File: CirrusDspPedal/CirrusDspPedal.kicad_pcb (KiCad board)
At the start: 2 copper layers, 112.5 x 86.4 mm, 5 parts

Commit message: updates
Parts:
- removed the REF** at (198.8, 62.2)
- removed the REF** at (111.1, 62.2)
- removed the REF** at (111.1, 135.9)
- added C1: 100nF, Capacitor_SMD:C_0805_2012Metric_Pad1.15x1.40mm_HandSolder, F.Cu at (215.3, 126.4)
- added C10: 100nF, Capacitor_SMD:C_0805_2012Metric_Pad1.15x1.40mm_HandSolder, F.Cu at (74.3, 143.5)
- added C11: 1uF, Capacitor_SMD:C_0805_2012Metric_Pad1.15x1.40mm_HandSolder, F.Cu at (79.4, 143.5)
- added C12: 3.3uF, Capacitor_SMD:C_0805_2012Metric_Pad1.15x1.40mm_HandSolder, F.Cu at (67.3, 121.3)
- added C13: 10uF, Capacitor_SMD:C_0805_2012Metric_Pad1.15x1.40mm_HandSolder, F.Cu at (69.2, 143.5)
- added C14: 2.7nF, Capacitor_SMD:C_0805_2012Metric_Pad1.15x1.40mm_HandSolder, F.Cu at (72.2, 120.9)
- added C15: 100nF, Capacitor_SMD:C_0805_2012Metric_Pad1.15x1.40mm_HandSolder, F.Cu at (76.4, 135.7)
- added C16: 100nF, Capacitor_SMD:C_0805_2012Metric_Pad1.15x1.40mm_HandSolder, F.Cu at (71.7, 135.7)
- added C17: 100nF, Capacitor_SMD:C_0805_2012Metric_Pad1.15x1.40mm_HandSolder, F.Cu at (71.7, 138.7)
- added C18: 100nF, Capacitor_SMD:C_0805_2012Metric_Pad1.15x1.40mm_HandSolder, F.Cu at (141.6, -22.2)
- added C19: 100nF, Capacitor_SMD:C_0805_2012Metric_Pad1.15x1.40mm_HandSolder, F.Cu at (141.6, -19.7)
- added C2: 1uF, Capacitor_SMD:C_0805_2012Metric_Pad1.15x1.40mm_HandSolder, F.Cu at (215.3, 123.8)
- added C20: 100nF, Capacitor_SMD:C_0805_2012Metric_Pad1.15x1.40mm_HandSolder, F.Cu at (141.6, -17.1)
- added C21: 100nF, Capacitor_SMD:C_0805_2012Metric_Pad1.15x1.40mm_HandSolder, F.Cu at (141.6, -14.6)
- added C22: 2.2uF, Capacitor_SMD:C_0805_2012Metric_Pad1.15x1.40mm_HandSolder, F.Cu at (146.7, -22.2)
- added C28: 1uF, Capacitor_SMD:C_1206_3216Metric_Pad1.42x1.75mm_HandSolder, F.Cu at (130.8, 44.5)
- added C29: 1uF, Capacitor_SMD:C_1206_3216Metric_Pad1.42x1.75mm_HandSolder, F.Cu at (123.2, 38.1)
- added C3: 10uF, Capacitor_SMD:C_0805_2012Metric_Pad1.15x1.40mm_HandSolder, F.Cu at (215.3, 128.9)
- added C30: 180pF C0G, Capacitor_SMD:C_0805_2012Metric_Pad1.15x1.40mm_HandSolder, F.Cu at (176.5, 39.4)
- added C31: 180pF C0G, Capacitor_SMD:C_0805_2012Metric_Pad1.15x1.40mm_HandSolder, F.Cu at (235.6, 77.5)
- added C32: 180pF C0G, Capacitor_SMD:C_0805_2012Metric_Pad1.15x1.40mm_HandSolder, F.Cu at (76.2, 71.8)
- added C33: 2.2uF, Capacitor_SMD:C_0805_2012Metric_Pad1.15x1.40mm_HandSolder, F.Cu at (146.7, -18.4)
- added C4: 1uF, Capacitor_SMD:C_0805_2012Metric_Pad1.15x1.40mm_HandSolder, F.Cu at (228.0, 130.3)
- added C5: 180pF C0G, Capacitor_SMD:C_0805_2012Metric_Pad1.15x1.40mm_HandSolder, F.Cu at (228.0, 132.7)
- added C6: 100nF, Capacitor_SMD:C_0805_2012Metric_Pad1.15x1.40mm_HandSolder, F.Cu at (215.3, 131.4)
- added C7: 100nF, Capacitor_SMD:C_0805_2012Metric_Pad1.15x1.40mm_HandSolder, F.Cu at (232.2, 138.3)
- added C8: 100nF, Capacitor_SMD:C_0805_2012Metric_Pad1.15x1.40mm_HandSolder, F.Cu at (237.0, 138.3)
- added C9: 100nF, Capacitor_SMD:C_0805_2012Metric_Pad1.15x1.40mm_HandSolder, F.Cu at (237.0, 141.2)
- added D1: D_Schottky, Diode_SMD:D_SOD-123F, F.Cu at (121.9, 44.5)
- added D2: 1N4148, Diode_SMD:D_SOD-123F, F.Cu at (143.9, 105.6)
- added FB1: 600, Inductor_SMD:L_0805_2012Metric_Pad1.15x1.40mm_HandSolder, F.Cu at (232.2, 141.2)
- added FB2: 600, Inductor_SMD:L_0805_2012Metric_Pad1.15x1.40mm_HandSolder, F.Cu at (76.4, 138.7)
- added J1: MonoJack2Switch, NeutrikNRJ:NRJxHx_NOTAB, F.Cu at (193.7, 110.5)
- added J2: MonoJack2Switch, NeutrikNRJ:NRJxHx_NOTAB, F.Cu at (103.5, 110.5)
- added J3: Conn_02x05_Odd_Even, Connector_PinHeader_1.27mm:PinHeader_2x05_P1.27mm_Vertical_SMD, F.Cu at (113.4, -18.9)
- added J4: Barrel_Jack_Switch, Connector_BarrelJack:BarrelJack_Horizontal, F.Cu at (129.5, 68.6)
- added J5: MonoJack2Switch, NeutrikNRJ:NRJxHx_NOTAB, F.Cu at (171.4, 66.7)
- added J6: Micro_SD_Card_Det, Connector_Card:microSD_HC_Molex_104031-0811, F.Cu at (230.5, -22.2)
- added J7: Conn_01x01, TestPoint:TestPoint_Pad_2.0x2.0mm, F.Cu at (259.7, -15.9)
- added JP1: Jumper_NC_Small, Jumper:SolderJumper-2_P1.3mm_Bridged_Pad1.0x1.5mm, F.Cu at (230.5, -4.45)
- added K1: HFD4/5-S, Relay_SMD:Relay_Fujitsu_FTR-B3S, F.Cu at (148.3, 113.3)
- added L1: 600, Inductor_SMD:L_0805_2012Metric_Pad1.15x1.40mm_HandSolder, F.Cu at (146.7, -15.9)
- added LED1: LED_RABG, LED_THT:LED_D5.0mm-4_RGB_Wide_Pins, F.Cu at (81.9, 3.17)
- added LED2: LED_RABG, LED_THT:LED_D5.0mm-4_RGB_Wide_Pins, F.Cu at (111.1, 1.91)
- added R1: 5K1, Resistor_SMD:R_0805_2012Metric_Pad1.15x1.40mm_HandSolder, F.Cu at (222.9, 132.7)
- added R10: 1K, Resistor_SMD:R_0805_2012Metric_Pad1.15x1.40mm_HandSolder, F.Cu at (156.8, 151.1)
- added R11: 100R, Resistor_SMD:R_0805_2012Metric_Pad1.15x1.40mm_HandSolder, F.Cu at (235.6, 81.3)
- added R12: 100R, Resistor_SMD:R_0805_2012Metric_Pad1.15x1.40mm_HandSolder, F.Cu at (76.2, 76.8)
- added R13: 50R, Resistor_SMD:R_0805_2012Metric_Pad1.15x1.40mm_HandSolder, F.Cu at (235.6, 85.1)
- added R14: 50R, Resistor_SMD:R_0805_2012Metric_Pad1.15x1.40mm_HandSolder, F.Cu at (76.2, 80.6)
- added R15: 1K, Resistor_SMD:R_0805_2012Metric_Pad1.15x1.40mm_HandSolder, F.Cu at (255.9, 81.9)
- added R16: 1K, Resistor_SMD:R_0805_2012Metric_Pad1.15x1.40mm_HandSolder, F.Cu at (47.6, 76.8)
- added R17: 220R, Resistor_SMD:R_0805_2012Metric_Pad1.15x1.40mm_HandSolder, F.Cu at (75.6, -0.64)
- added R18: 220R, Resistor_SMD:R_0805_2012Metric_Pad1.15x1.40mm_HandSolder, F.Cu at (75.6, 3.17)
- added R19: 220R, Resistor_SMD:R_0805_2012Metric_Pad1.15x1.40mm_HandSolder, F.Cu at (75.6, 6.99)
- added R2: 5K1, Resistor_SMD:R_0805_2012Metric_Pad1.15x1.40mm_HandSolder, F.Cu at (222.9, 130.2)
- added R20: 220R, Resistor_SMD:R_0805_2012Metric_Pad1.15x1.40mm_HandSolder, F.Cu at (104.8, -1.91)
- added R21: 220R, Resistor_SMD:R_0805_2012Metric_Pad1.15x1.40mm_HandSolder, F.Cu at (104.8, 1.91)
- added R22: 220R, Resistor_SMD:R_0805_2012Metric_Pad1.15x1.40mm_HandSolder, F.Cu at (104.8, 5.71)
- added R23: 10K, Resistor_SMD:R_0805_2012Metric_Pad1.15x1.40mm_HandSolder, F.Cu at (225.0, -11.4)
- added R24: 47K, Resistor_SMD:R_0805_2012Metric_Pad1.15x1.40mm_HandSolder, F.Cu at (225.0, -8.46)
- added R25: 47K, Resistor_SMD:R_0805_2012Metric_Pad1.15x1.40mm_HandSolder, F.Cu at (229.8, -11.4)
- added R26: 47K, Resistor_SMD:R_0805_2012Metric_Pad1.15x1.40mm_HandSolder, F.Cu at (234.3, -8.26)
- added R27: 47K, Resistor_SMD:R_0805_2012Metric_Pad1.15x1.40mm_HandSolder, F.Cu at (229.8, -8.46)
- added R28: 47K, Resistor_SMD:R_0805_2012Metric_Pad1.15x1.40mm_HandSolder, F.Cu at (234.5, -11.4)
- added R3: 10K, Resistor_SMD:R_0805_2012Metric_Pad1.15x1.40mm_HandSolder, F.Cu at (228.0, 123.8)
- added R4: 1R 1%, Resistor_SMD:R_0805_2012Metric_Pad1.15x1.40mm_HandSolder, F.Cu at (241.7, 138.3)
- added R5: 10K, Resistor_SMD:R_0805_2012Metric_Pad1.15x1.40mm_HandSolder, F.Cu at (72.2, 123.9)
- added R6: 470 1%, Resistor_SMD:R_0805_2012Metric_Pad1.15x1.40mm_HandSolder, F.Cu at (76.9, 120.9)
- added R7: 1R 1%, Resistor_SMD:R_0805_2012Metric_Pad1.15x1.40mm_HandSolder, F.Cu at (81.2, 135.7)
- added R8: 50R, Resistor_SMD:R_0805_2012Metric_Pad1.15x1.40mm_HandSolder, F.Cu at (176.5, 36.8)
- added R9: 1K, Resistor_SMD:R_0805_2012Metric_Pad1.15x1.40mm_HandSolder, F.Cu at (142.9, 150.5)
- added REF**: MountingHole_4mm_Pad_Via, MountingHole:MountingHole_4mm_Pad_Via, F.Cu at (192.4, 60.9)
- added REF**: MountingHole_4mm_Pad_Via, MountingHole:MountingHole_4mm_Pad_Via, F.Cu at (104.8, 60.9)
- added REF**: MountingHole_4mm_Pad_Via, MountingHole:MountingHole_4mm_Pad_Via, F.Cu at (104.8, 134.6)
- added RV1: R_POT, Potentiometer_THT:Potentiometer_Alps_RK09L_Single_Vertical, F.Cu at (226.7, 87.6)
- added RV2: R_POT, Potentiometer_THT:Potentiometer_Alps_RK09L_Single_Vertical, F.Cu at (67.3, 81.9)
- added SW1: P26L-1D-RND MTL, Connector_PinSocket_2.54mm:PinSocket_1x02_P2.54mm_Vertical, F.Cu at (144.8, 134.6)
- added SW2: P26L-1D-RND MTL, Connector_PinSocket_2.54mm:PinSocket_1x02_P2.54mm_Vertical, F.Cu at (153.7, 135.9)
- added SW3: SW_SPST, custom_sw:SW_SPDT_W6.86MM_L12.7MM_P4.8MM_D2MM, F.Cu at (250.1, 81.5)
- added SW4: SW_SPST, custom_sw:SW_SPDT_W6.86MM_L12.7MM_P4.8MM_D2MM, F.Cu at (41.9, 77.5)
- added U1: CS5343, Package_SO:TSSOP-10_3x3mm_P0.5mm, F.Cu at (225.4, 140.3)
- added U2: 74AHC1G126, Package_TO_SOT_SMD:SOT-23-5_HandSoldering, F.Cu at (223.4, 123.8)
- added U3: CS4344, Package_SO:TSSOP-10_3x3mm_P0.5mm, F.Cu at (75.2, 130.2)
- added U5: MCP1700-3302E_SOT23, Package_TO_SOT_SMD:SOT-23, F.Cu at (133.3, 36.8)
- added U6: MCP601-xOT, Package_TO_SOT_SMD:SOT-23-5, F.Cu at (171.4, 38.1)
- added U7: STM32F405RGTx, Package_QFP:LQFP-64_10x10mm_P0.5mm, F.Cu at (130.7, -18.9)
- moved REF** 6.48 mm to (148.6, 97.8)
- moved REF** 6.48 mm to (192.4, 134.6)
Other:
- outline, holes or cut-outs redrawn

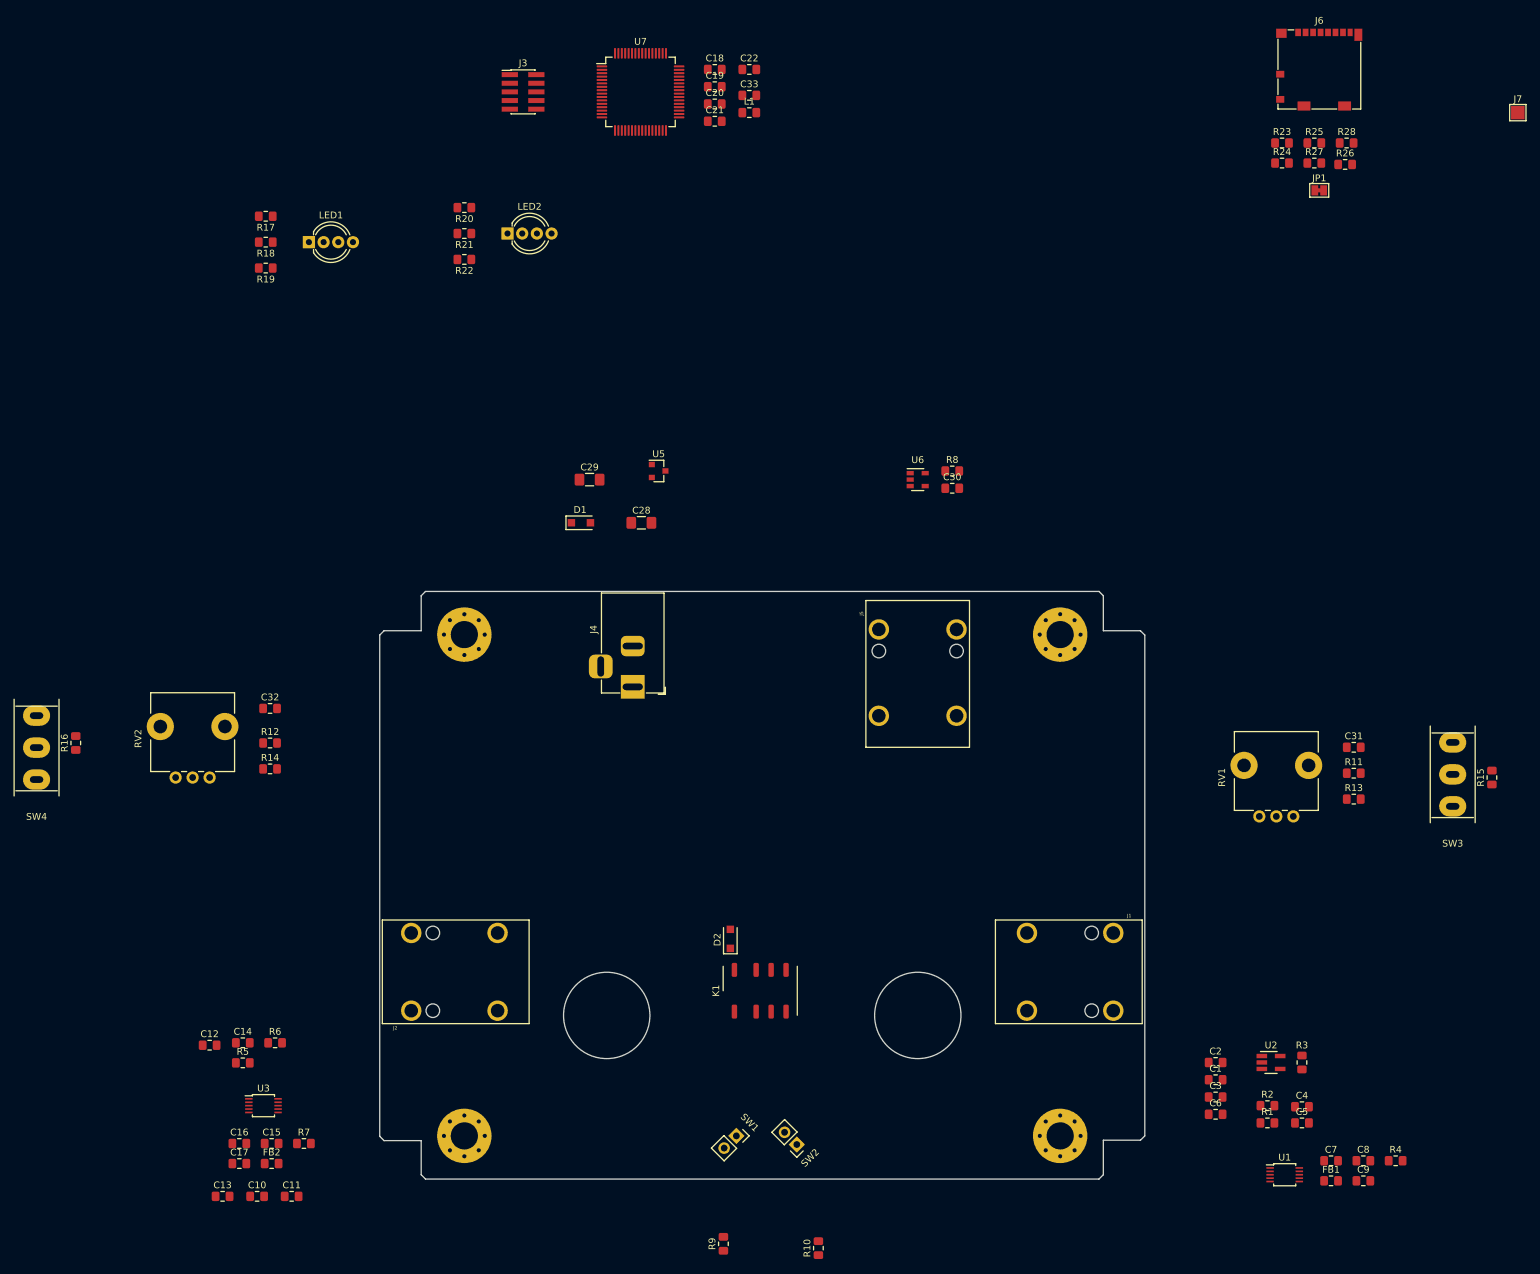
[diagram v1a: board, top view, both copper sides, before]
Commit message: finished RevA layout
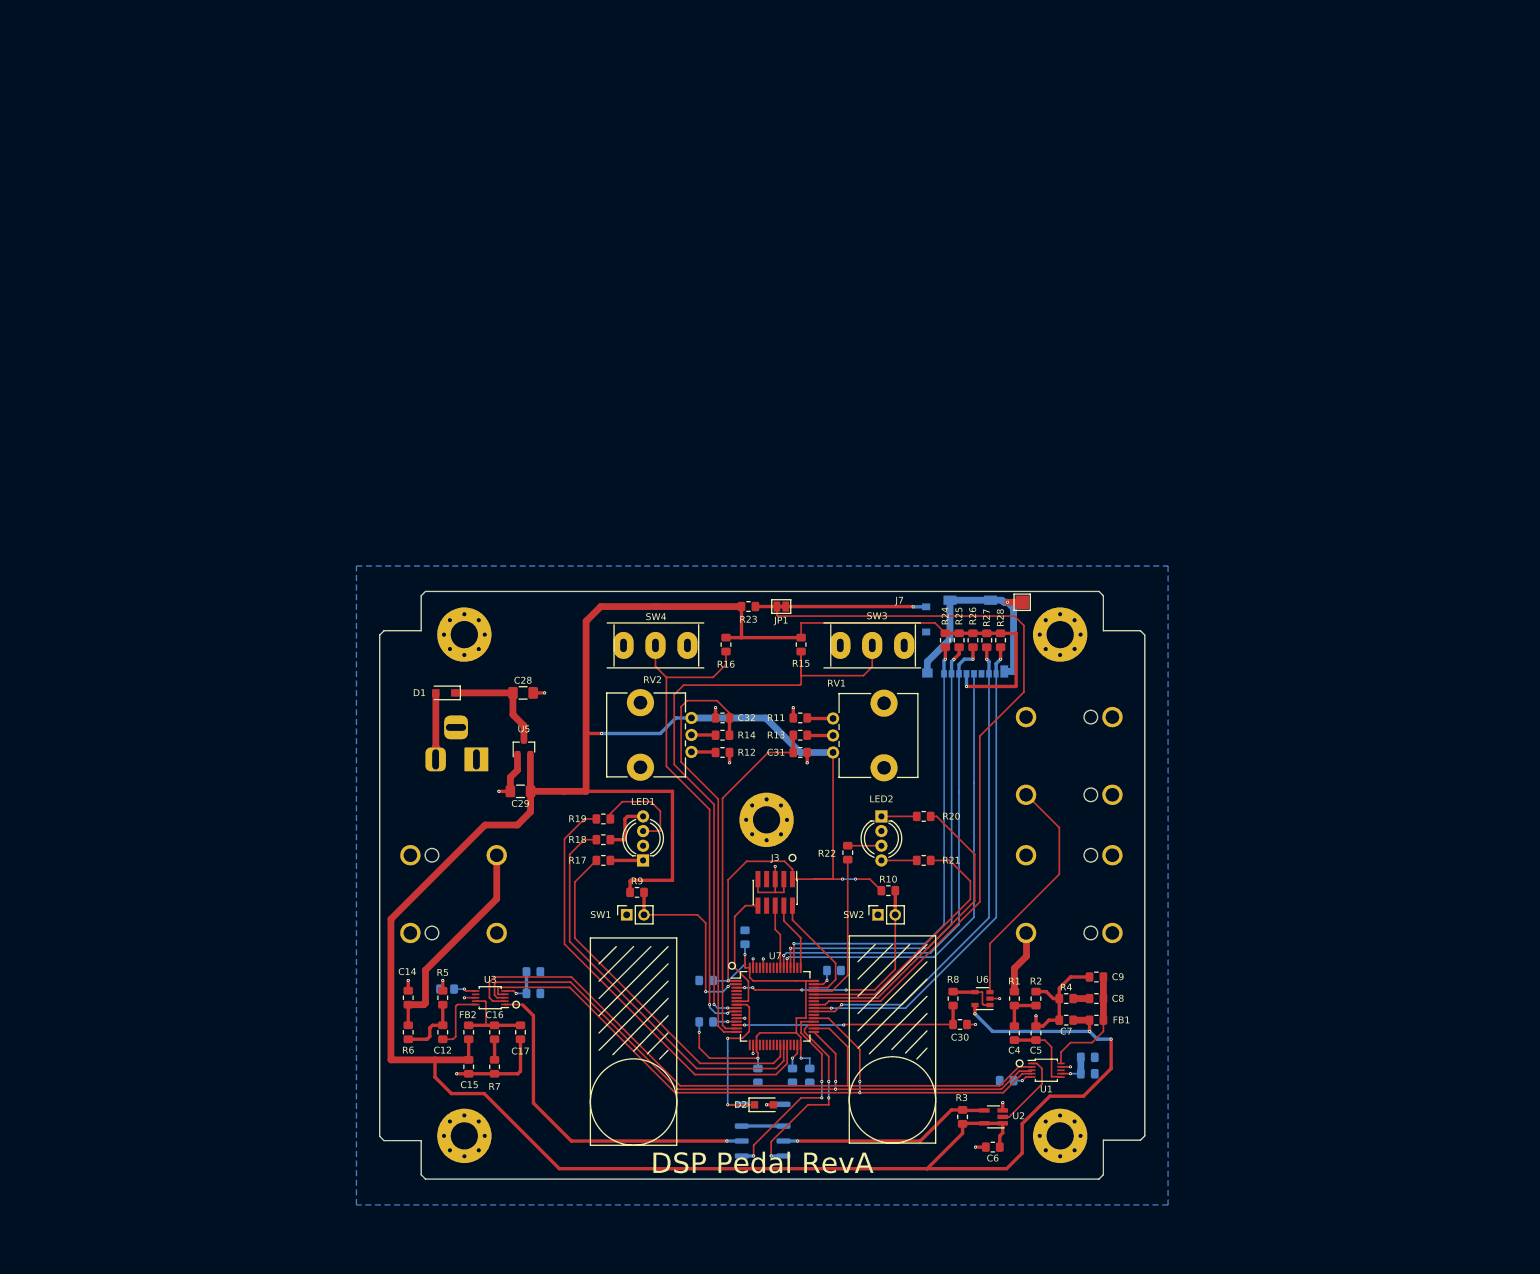
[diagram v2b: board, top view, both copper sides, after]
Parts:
- added REF**: MountingHole_4mm_Pad_Via, MountingHole:MountingHole_4mm_Pad_Via, F.Cu at (149.2, 88.1)
- C1, C10, C11, C13, C18, C19, C2, C20, C21, C22, C3, C33, J1, J2, J4, J5, J6, K1, L1: moved to B.Cu
- moved C22 148.1 mm to (153.0, 125.7), turned to 90 degrees
- moved C19 146.1 mm to (155.6, 125.7), turned to 270 degrees
- moved C20 143.0 mm to (148.0, 125.7), turned to 270 degrees
- moved U7 135.9 mm to (150.5, 115.6)
- moved C18 134.0 mm to (140.3, 111.8), turned to 180 degrees
- moved L1 133.9 mm to (140.3, 117.9)
- moved C33 129.3 mm to (159.1, 110.3), turned to 180 degrees
- moved J3 123.4 mm to (150.5, 98.8), turned to 270 degrees
- moved C21 120.1 mm to (146.1, 105.4), turned to 90 degrees
- moved R21 114.3 mm to (172.3, 94.1), turned to 0 degrees
- moved R20 112.2 mm to (172.3, 87.6), turned to 0 degrees
- moved R17 107.0 mm to (125.2, 94.1)
- moved R23 104.0 mm to (146.6, 56.8)
- moved R22 103.9 mm to (161.2, 93.0), turned to 270 degrees
- moved R15 103.5 mm to (154.3, 62.4), turned to 270 degrees
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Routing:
- net +3V3: track 0.00 -> 562.4 mm, vias 0 -> 12
- net /MicroSD/uSD_Detect: track 0.00 -> 115.4 mm
- net /InputSignal/ADIN_SCLK: track 0.00 -> 104.5 mm
- net /InputSignal/ADIN_MCLK: track 0.00 -> 103.1 mm, vias 0 -> 2
- net /InputSignal/ADIN_LRCK: track 0.00 -> 99.9 mm, vias 0 -> 2
- net /ExtInput/UserSwitchA_IN: track 0.00 -> 93.4 mm, vias 0 -> 2
- net GND: track 0.00 -> 77.6 mm, vias 0 -> 22
- net /MicroSD/uSD_D1: track 0.00 -> 72.7 mm, vias 0 -> 2
- net /ExtInput/UserSwitchB_IN: track 0.00 -> 72.4 mm, vias 0 -> 2
- net /MicroSD/uSD_CMD: track 0.00 -> 71.8 mm, vias 0 -> 2
- net /MicroSD/uSD_D0: track 0.00 -> 71.6 mm, vias 0 -> 2
- net /MicroSD/uSD_D3: track 0.00 -> 69.2 mm, vias 0 -> 2
- net /MicroSD/uSD_D2: track 0.00 -> 67.9 mm, vias 0 -> 2
- net /MicroSD/uSD_CLK: track 0.00 -> 67.1 mm, vias 0 -> 1
- net /SignalProcessing/LEDA_B: track 0.00 -> 65.5 mm
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- added copper zone on B.Cu, net GND
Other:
- outline, holes or cut-outs redrawn
- net class Default: clearance 0.2 -> 0.127; trace_width 0.25 -> 0.127
- rule trace_clearance: 0.2 -> 0.127
- rule trace_min: 0.2 -> 0.127
- rule via_min_drill: 0.3 -> 0.2
- rule via_min_size: 0.4 -> 0.45
- board text added: "DSP Pedal RevA"

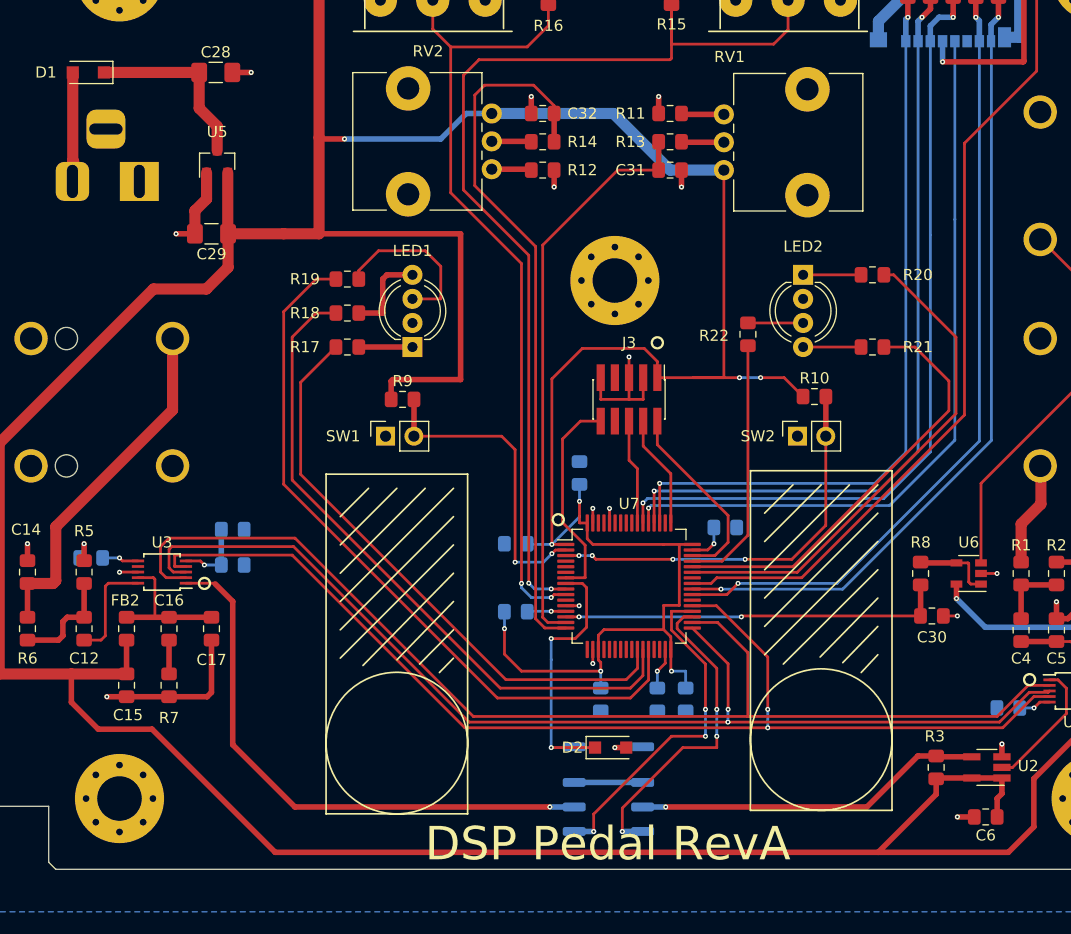
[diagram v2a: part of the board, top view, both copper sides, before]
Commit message: updated design and layout
- Changed LDO to 1703 (footprint unchanged)
- Changed THT LEDs from RAGB (incorrect) to RCGB (correct) symbol (footprint unchanged)
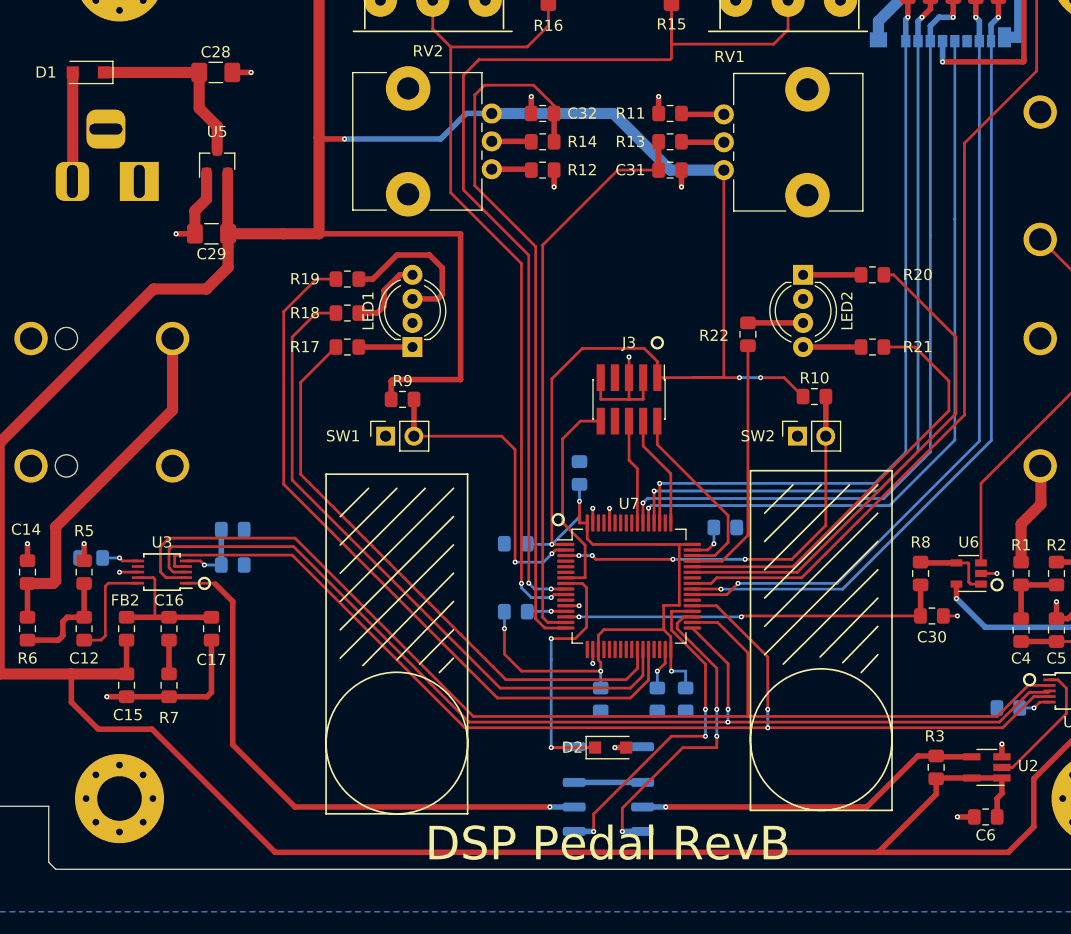
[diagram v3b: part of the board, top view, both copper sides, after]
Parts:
- removed the REF** at (149.2, 88.1)
- LED1, LED2: value LED_RABG -> LED_RCBG
- RV1, RV2: value R_POT -> RK09L1140A65
- U5: value MCP1700-3302E_SOT23 -> MCP1703T-3302E/CB
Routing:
- net Net-(D1-Pad2): track 8.04 -> 9.79 mm
- net Net-(LED1-Pad4): track 8.02 -> 7.06 mm
- net Net-(LED1-Pad3): track 14.9 -> 14.1 mm
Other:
- board text added: "DSP Pedal RevB"
- board text removed: "DSP Pedal RevA"
